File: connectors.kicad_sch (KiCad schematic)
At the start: 4 parts

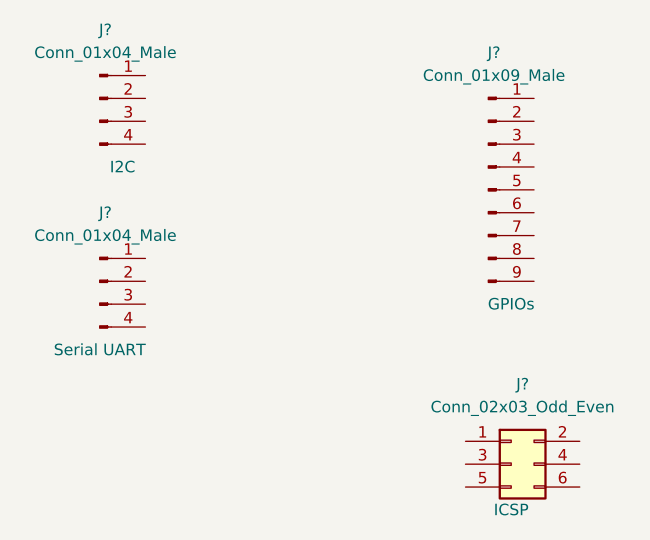
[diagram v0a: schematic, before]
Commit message: Added components values
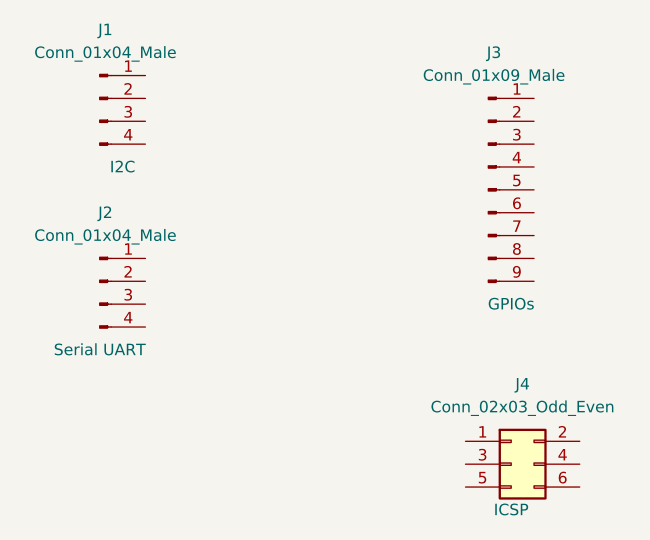
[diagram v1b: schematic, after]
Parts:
- gave numbers to parts that had none: 4
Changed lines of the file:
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@@
   (symbol (lib_id "Connector:Conn_01x04_Male") (at 60.96 35.56 0) (unit 1)
     (in_bom yes) (on_board yes)
-    (property "Reference" "J?" (id 0) (at 61.595 27.94 0))
+    (property "Reference" "J1" (id 0) (at 61.595 27.94 0))
     (property "Value" "Conn_01x04_Male" (id 1) (at 61.595 30.48 0))
     (property "Footprint" "" (id 2) (at 60.96 35.56 0)
@@
   (symbol (lib_id "Connector:Conn_01x09_Male") (at 104.14 45.72 0) (unit 1)
     (in_bom yes) (on_board yes)
-    (property "Reference" "J?" (id 0) (at 104.775 30.48 0))
+    (property "Reference" "J3" (id 0) (at 104.775 30.48 0))
     (property "Value" "Conn_01x09_Male" (id 1) (at 104.775 33.02 0))
     (property "Footprint" "" (id 2) (at 104.14 45.72 0)
@@
   (symbol (lib_id "Connector:Conn_01x04_Male") (at 60.96 55.88 0) (unit 1)
     (in_bom yes) (on_board yes)
-    (property "Reference" "J?" (id 0) (at 61.595 48.26 0))
+    (property "Reference" "J2" (id 0) (at 61.595 48.26 0))
     (property "Value" "Conn_01x04_Male" (id 1) (at 61.595 50.8 0))
     (property "Footprint" "" (id 2) (at 60.96 55.88 0)
@@
   (symbol (lib_id "Connector_Generic:Conn_02x03_Odd_Even") (at 106.68 76.2 0) (unit 1)
     (in_bom yes) (on_board yes)
-    (property "Reference" "J?" (id 0) (at 107.95 67.31 0))
+    (property "Reference" "J4" (id 0) (at 107.95 67.31 0))
     (property "Value" "Conn_02x03_Odd_Even" (id 1) (at 107.95 69.85 0))
     (property "Footprint" "" (id 2) (at 106.68 76.2 0)

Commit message: Completed symbol footpring associations
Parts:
- J1, J2: footprint (none) -> Connector_PinHeader_2.54mm:PinHeader_1x04_P2.54mm_Vertical
- J3: footprint (none) -> Connector_PinHeader_2.54mm:PinHeader_1x09_P2.54mm_Vertical
- J4: footprint (none) -> Connector_PinHeader_2.54mm:PinHeader_2x03_P2.54mm_Vertical
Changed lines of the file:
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@@
     (property "Reference" "J1" (id 0) (at 61.595 27.94 0))
     (property "Value" "Conn_01x04_Male" (id 1) (at 61.595 30.48 0))
-    (property "Footprint" "" (id 2) (at 60.96 35.56 0)
+    (property "Footprint" "Connector_PinHeader_2.54mm:PinHeader_1x04_P2.54mm_Vertical" (id 2) (at 60.96 35.56 0)
       (effects (font (size 1.27 1.27)) hide)
     )
@@
     (property "Reference" "J3" (id 0) (at 104.775 30.48 0))
     (property "Value" "Conn_01x09_Male" (id 1) (at 104.775 33.02 0))
-    (property "Footprint" "" (id 2) (at 104.14 45.72 0)
+    (property "Footprint" "Connector_PinHeader_2.54mm:PinHeader_1x09_P2.54mm_Vertical" (id 2) (at 104.14 45.72 0)
       (effects (font (size 1.27 1.27)) hide)
     )
@@
     (property "Reference" "J2" (id 0) (at 61.595 48.26 0))
     (property "Value" "Conn_01x04_Male" (id 1) (at 61.595 50.8 0))
-    (property "Footprint" "" (id 2) (at 60.96 55.88 0)
+    (property "Footprint" "Connector_PinHeader_2.54mm:PinHeader_1x04_P2.54mm_Vertical" (id 2) (at 60.96 55.88 0)
       (effects (font (size 1.27 1.27)) hide)
     )
@@
     (property "Reference" "J4" (id 0) (at 107.95 67.31 0))
     (property "Value" "Conn_02x03_Odd_Even" (id 1) (at 107.95 69.85 0))
-    (property "Footprint" "" (id 2) (at 106.68 76.2 0)
+    (property "Footprint" "Connector_PinHeader_2.54mm:PinHeader_2x03_P2.54mm_Vertical" (id 2) (at 106.68 76.2 0)
       (effects (font (size 1.27 1.27)) hide)
     )

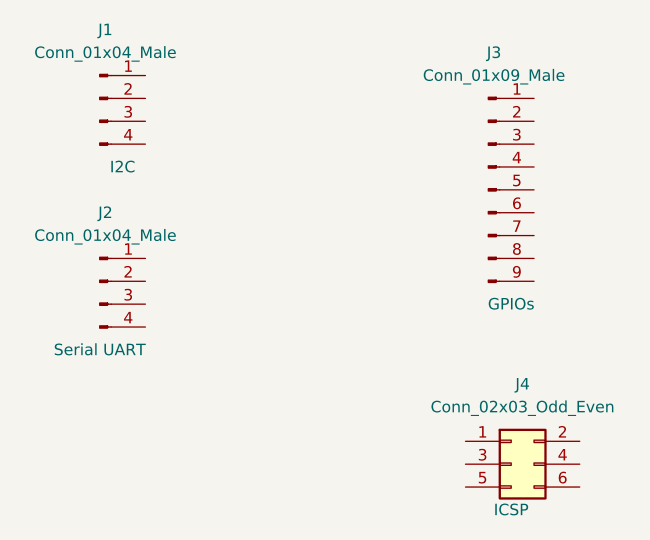
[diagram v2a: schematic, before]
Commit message: Completed wiring in all sheets
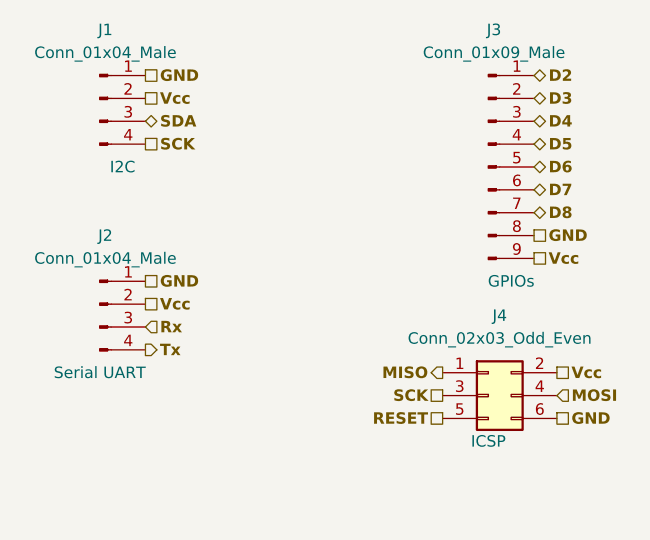
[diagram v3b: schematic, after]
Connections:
- net GND: now reaches J1.1 (Pin_1)
- net GND: now also J2.1 (Pin_1), J3.8 (Pin_8), J4.6 (Pin_6)
- net Vcc: now reaches J1.2 (Pin_2)
- net Vcc: now also J2.2 (Pin_2), J3.9 (Pin_9), J4.2 (Pin_2)
- net SDA: now reaches J1.3 (Pin_3)
- net SCK: now reaches J1.4 (Pin_4)
- net SCK: now also J4.3 (Pin_3)
- net D2: now reaches J3.1 (Pin_1)
- net D3: now reaches J3.2 (Pin_2)
- net D4: now reaches J3.3 (Pin_3)
- net D5: now reaches J3.4 (Pin_4)
- net D6: now reaches J3.5 (Pin_5)
- net D7: now reaches J3.6 (Pin_6)
- net D8: now reaches J3.7 (Pin_7)
- net Rx: now reaches J2.3 (Pin_3)
- net Tx: now reaches J2.4 (Pin_4)
- net MISO: now reaches J4.1 (Pin_1)
- net MOSI: now reaches J4.4 (Pin_4)
- net RESET: now reaches J4.5 (Pin_5)
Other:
- moved on the sheet: J2, J3, J4
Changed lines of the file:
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@@
 (kicad_sch (version 20211123) (generator eeschema)
   (paper "A4")
+  (hierarchical_label "GND" (shape passive) (at 109.22 50.8 0)
+    (effects (font (size 1.27 1.27) bold) (justify left))
+  )
+  (hierarchical_label "D6" (shape bidirectional) (at 109.22 43.18 0)
+    (effects (font (size 1.27 1.27) bold) (justify left))
+  )
+  (hierarchical_label "SCK" (shape passive) (at 66.04 40.64 0)
+    (effects (font (size 1.27 1.27) bold) (justify left))
+  )
+  (hierarchical_label "D3" (shape bidirectional) (at 109.22 35.56 0)
+    (effects (font (size 1.27 1.27) bold) (justify left))
+  )
+  (hierarchical_label "Rx" (shape input) (at 66.04 60.96 0)
+    (effects (font (size 1.27 1.27) bold) (justify left))
+  )
+  (hierarchical_label "RESET" (shape passive) (at 99.06 71.12 180)
+    (effects (font (size 1.27 1.27) bold) (justify right))
+  )
+  (hierarchical_label "D7" (shape bidirectional) (at 109.22 45.72 0)
+    (effects (font (size 1.27 1.27) bold) (justify left))
+  )
+  (hierarchical_label "Tx" (shape output) (at 66.04 63.5 0)
+    (effects (font (size 1.27 1.27) bold) (justify left))
+  )
+  (hierarchical_label "SCK" (shape passive) (at 99.06 68.58 180)
+    (effects (font (size 1.27 1.27) bold) (justify right))
+  )
+  (hierarchical_label "Vcc" (shape passive) (at 66.04 58.42 0)
+    (effects (font (size 1.27 1.27) bold) (justify left))
+  )
+  (hierarchical_label "D4" (shape bidirectional) (at 109.22 38.1 0)
+    (effects (font (size 1.27 1.27) bold) (justify left))
+  )
+  (hierarchical_label "D2" (shape bidirectional) (at 109.22 33.02 0)
+    (effects (font (size 1.27 1.27) bold) (justify left))
+  )
+  (hierarchical_label "GND" (shape passive) (at 66.04 55.88 0)
+    (effects (font (size 1.27 1.27) bold) (justify left))
+  )
+  (hierarchical_label "Vcc" (shape passive) (at 66.04 35.56 0)
+    (effects (font (size 1.27 1.27) bold) (justify left))
+  )
+  (hierarchical_label "SDA" (shape bidirectional) (at 66.04 38.1 0)
+    (effects (font (size 1.27 1.27) bold) (justify left))
+  )
+  (hierarchical_label "GND" (shape passive) (at 66.04 33.02 0)
+    (effects (font (size 1.27 1.27) bold) (justify left))
+  )
+  (hierarchical_label "D8" (shape bidirectional) (at 109.22 48.26 0)
+    (effects (font (size 1.27 1.27) bold) (justify left))
+  )
+  (hierarchical_label "Vcc" (shape passive) (at 109.22 53.34 0)
+    (effects (font (size 1.27 1.27) bold) (justify left))
+  )
+  (hierarchical_label "MOSI" (shape input) (at 111.76 68.58 0)
+    (effects (font (size 1.27 1.27) bold) (justify left))
+  )
+  (hierarchical_label "Vcc" (shape passive) (at 111.76 66.04 0)
+    (effects (font (size 1.27 1.27) bold) (justify left))
+  )
+  (hierarchical_label "D5" (shape bidirectional) (at 109.22 40.64 0)
+    (effects (font (size 1.27 1.27) bold) (justify left))
+  )
+  (hierarchical_label "MISO" (shape output) (at 99.06 66.04 180)
+    (effects (font (size 1.27 1.27) bold) (justify right))
+  )
+  (hierarchical_label "GND" (shape passive) (at 111.76 71.12 0)
+    (effects (font (size 1.27 1.27) bold) (justify left))
+  )
   (symbol (lib_id "Connector:Conn_01x04_Male") (at 60.96 35.56 0) (unit 1)
     (in_bom yes) (on_board yes)
@@
     (pin "4")
   )
-  (symbol (lib_id "Connector:Conn_01x09_Male") (at 104.14 45.72 0) (unit 1)
+  (symbol (lib_id "Connector:Conn_01x09_Male") (at 104.14 43.18 0) (unit 1)
     (in_bom yes) (on_board yes)
-    (property "Reference" "J3" (id 0) (at 104.775 30.48 0))
-    (property "Value" "Conn_01x09_Male" (id 1) (at 104.775 33.02 0))
-    (property "Footprint" "Connector_PinHeader_2.54mm:PinHeader_1x09_P2.54mm_Vertical" (id 2) (at 104.14 45.72 0)
+    (property "Reference" "J3" (id 0) (at 104.775 27.94 0))
+    (property "Value" "Conn_01x09_Male" (id 1) (at 104.775 30.48 0))
+    (property "Footprint" "Connector_PinHeader_2.54mm:PinHeader_1x09_P2.54mm_Vertical" (id 2) (at 104.14 43.18 0)
       (effects (font (size 1.27 1.27)) hide)
     )
-    (property "Datasheet" "~" (id 3) (at 104.14 45.72 0)
+    (property "Datasheet" "~" (id 3) (at 104.14 43.18 0)
       (effects (font (size 1.27 1.27)) hide)
     )
-    (property "Purpose" "GPIOs" (id 4) (at 106.68 58.42 0))
+    (property "Purpose" "GPIOs" (id 4) (at 106.68 55.88 0))
     (pin "1")
     (pin "2")
@@
     (pin "9")
   )
-  (symbol (lib_id "Connector:Conn_01x04_Male") (at 60.96 55.88 0) (unit 1)
+  (symbol (lib_id "Connector:Conn_01x04_Male") (at 60.96 58.42 0) (unit 1)
     (in_bom yes) (on_board yes)
-    (property "Reference" "J2" (id 0) (at 61.595 48.26 0))
-    (property "Value" "Conn_01x04_Male" (id 1) (at 61.595 50.8 0))
-    (property "Footprint" "Connector_PinHeader_2.54mm:PinHeader_1x04_P2.54mm_Vertical" (id 2) (at 60.96 55.88 0)
+    (property "Reference" "J2" (id 0) (at 61.595 50.8 0))
+    (property "Value" "Conn_01x04_Male" (id 1) (at 61.595 53.34 0))
+    (property "Footprint" "Connector_PinHeader_2.54mm:PinHeader_1x04_P2.54mm_Vertical" (id 2) (at 60.96 58.42 0)
       (effects (font (size 1.27 1.27)) hide)
     )
-    (property "Datasheet" "~" (id 3) (at 60.96 55.88 0)
+    (property "Datasheet" "~" (id 3) (at 60.96 58.42 0)
       (effects (font (size 1.27 1.27)) hide)
     )
-    (property "Purpose" "Serial UART" (id 4) (at 60.96 63.5 0))
+    (property "Purpose" "Serial UART" (id 4) (at 60.96 66.04 0))
     (pin "1")
     (pin "2")
@@
     (pin "4")
   )
-  (symbol (lib_id "Connector_Generic:Conn_02x03_Odd_Even") (at 106.68 76.2 0) (unit 1)
+  (symbol (lib_id "Connector_Generic:Conn_02x03_Odd_Even") (at 104.14 68.58 0) (unit 1)
     (in_bom yes) (on_board yes)
-    (property "Reference" "J4" (id 0) (at 107.95 67.31 0))
-    (property "Value" "Conn_02x03_Odd_Even" (id 1) (at 107.95 69.85 0))
-    (property "Footprint" "Connector_PinHeader_2.54mm:PinHeader_2x03_P2.54mm_Vertical" (id 2) (at 106.68 76.2 0)
+    (property "Reference" "J4" (id 0) (at 105.41 59.69 0))
+    (property "Value" "Conn_02x03_Odd_Even" (id 1) (at 105.41 62.23 0))
+    (property "Footprint" "Connector_PinHeader_2.54mm:PinHeader_2x03_P2.54mm_Vertical" (id 2) (at 104.14 68.58 0)
       (effects (font (size 1.27 1.27)) hide)
     )
-    (property "Datasheet" "~" (id 3) (at 106.68 76.2 0)
+    (property "Datasheet" "~" (id 3) (at 104.14 68.58 0)
       (effects (font (size 1.27 1.27)) hide)
     )
-    (property "Field4" "ICSP" (id 4) (at 106.68 81.28 0))
+    (property "Field4" "ICSP" (id 4) (at 104.14 73.66 0))
     (pin "1")
     (pin "2")
